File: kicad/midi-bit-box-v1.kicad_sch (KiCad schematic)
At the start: 60 parts, among them IC1 LM386, IC2 DIP14, K1 TQ2-L-5V, Q1 2N3904, Q2 2N3906, Q3 2N3904, Q4 2N3904, U1 AY-3-8910, U2 L78L09_TO92, U3 NE555P

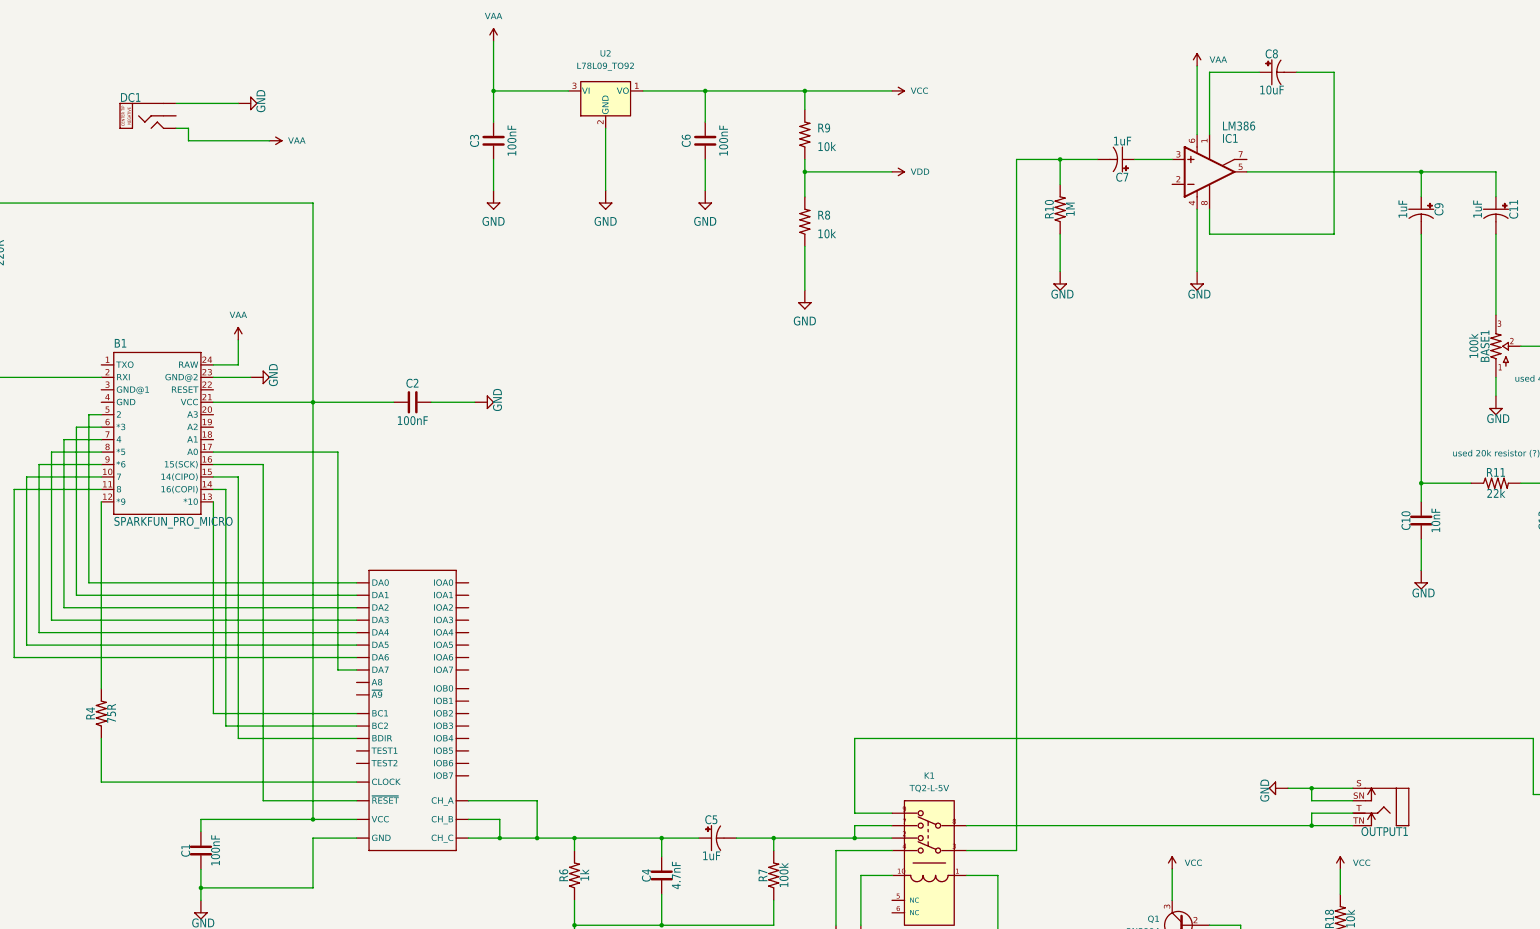
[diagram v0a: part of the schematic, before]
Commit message: Add files via upload
updated pwr/audio jacks and design rules
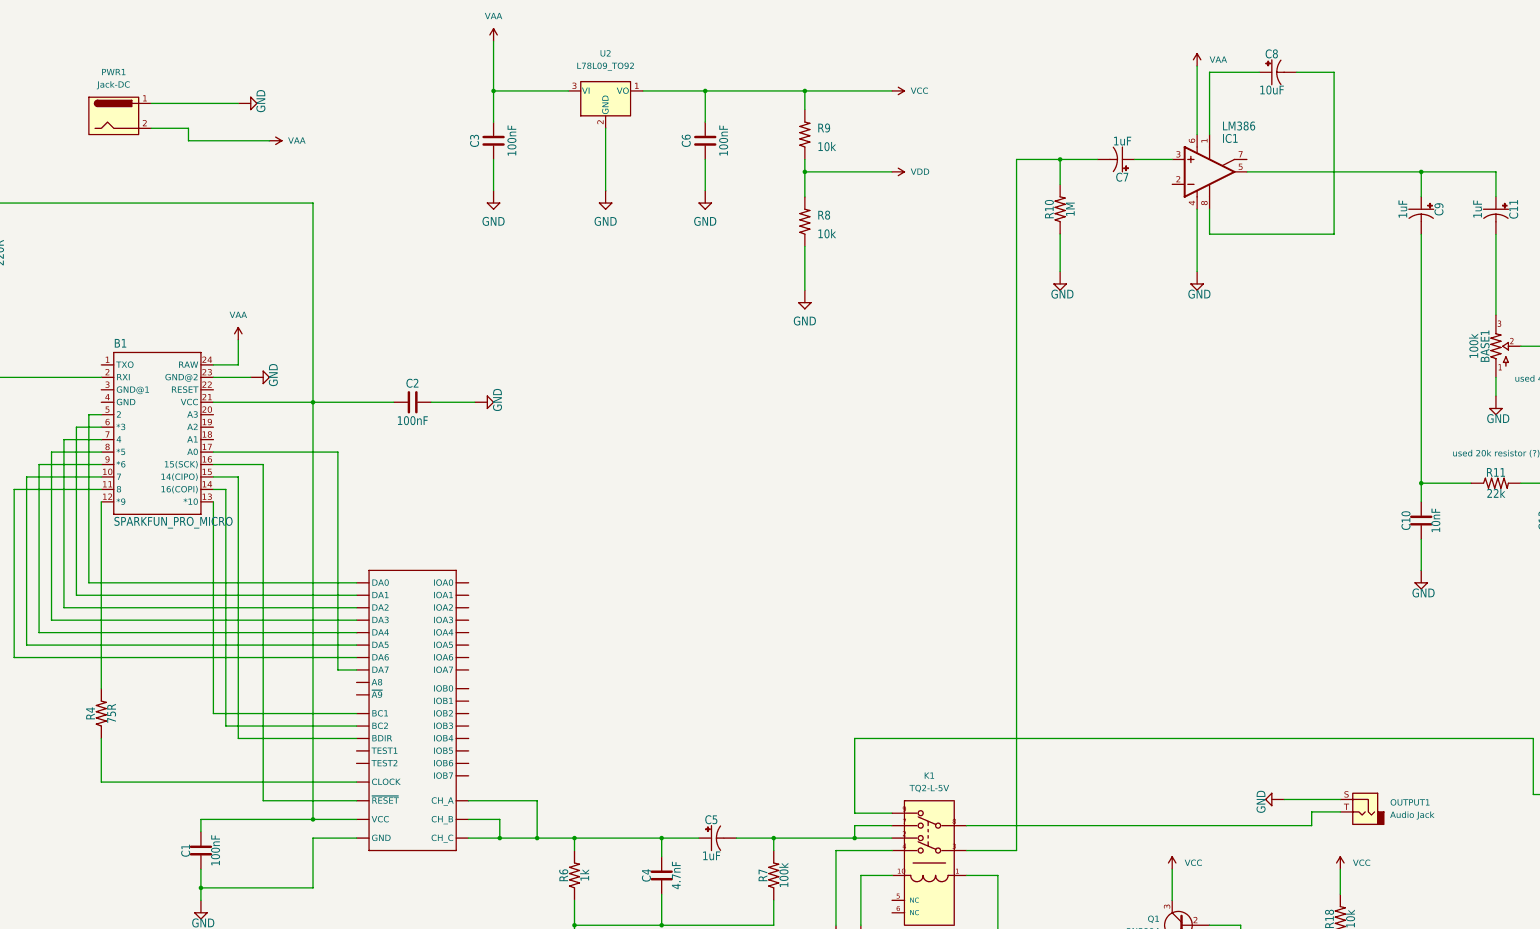
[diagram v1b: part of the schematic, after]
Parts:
- removed DC1: DC_TRS_PADS, midi-bit-box-v1:DC_TRS, symbol midi-bit-box-v1-eagle-import:DC_TRS_PADS
- removed OUTPUT1: SWITCHED_MONO_PADS, midi-bit-box-v1:4PADS, symbol midi-bit-box-v1-eagle-import:SWITCHED_MONO_PADS
- added OUTPUT1: Audio Jack, midi-bit-box-v1:2PADS, symbol Connector:AudioJack2
- added PWR1: Jack-DC, midi-bit-box-v1:DC_TS, symbol Connector:Jack-DC
- Q1, Q2, Q3, Q4, U2: footprint Package_TO_SOT_THT:TO-92_Inline -> midi-bit-box-v1:TO-92-djk-custom
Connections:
- net GND: now also OUTPUT1.S, PWR1.1
- net VAA: now also PWR1.2
- net at K1.8: now also OUTPUT1.T

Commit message: added dual LED
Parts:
- removed D5: LED.2, midi-bit-box-v1:3MM_1, symbol midi-bit-box-v1-eagle-import:LED.2
- added D2: LED_Dual_KAK, LED_THT:LED_D5.0mm-3, symbol Device:LED_Dual_KAK
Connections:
- net GND: now also D2.1 (K1)
- net at R17.1: now also D2.2 (A)
- net at Q4.3 (C): now also D2.3 (K2)
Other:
- moved on the sheet: R17
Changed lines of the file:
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@@
+    (stroke (width 0) (type default) (color 0 0 0 0))
+  )
+  (wire (pts (xy 375.666 244.856) (xy 397.51 244.856))
     (stroke (width 0) (type default) (color 0 0 0 0))
   )
@@
     (stroke (width 0) (type default) (color 0 0 0 0))
   )
-  (wire (pts (xy 342.9 245.11) (xy 355.6 245.11))
+  (wire (pts (xy 331.978 242.316) (xy 344.678 242.316))
     (stroke (width 0) (type default) (color 0 0 0 0))
   )
@@
     (stroke (width 0) (type default) (color 0 0 0 0))
   )
-  (wire (pts (xy 365.76 245.11) (xy 375.92 245.11))
-    (stroke (width 0) (type default) (color 0 0 0 0))
-  )
   (wire (pts (xy 139.7 120.65) (xy 139.7 86.36))
     (stroke (width 0) (type default) (color 0 0 0 0))
@@
     (stroke (width 0) (type default) (color 0 0 0 0))
   )
+  (wire (pts (xy 354.838 242.316) (xy 360.426 242.316))
+    (stroke (width 0) (type default) (color 0 0 0 0))
+  )
   (wire (pts (xy 196.85 130.81) (xy 129.54 130.81))
     (stroke (width 0) (type default) (color 0 0 0 0))
@@
     (stroke (width 0) (type default) (color 0 0 0 0))
   )
-  (wire (pts (xy 397.51 245.11) (xy 397.51 248.92))
+  (wire (pts (xy 397.51 244.856) (xy 397.51 248.92))
     (stroke (width 0) (type default) (color 0 0 0 0))
   )
@@
     (stroke (width 0) (type default) (color 0 0 0 0))
   )
+  (wire (pts (xy 375.666 239.776) (xy 382.778 239.776))
+    (stroke (width 0) (type default) (color 0 0 0 0))
+  )
   (wire (pts (xy 490.22 181.61) (xy 506.73 181.61))
     (stroke (width 0) (type default) (color 0 0 0 0))
@@
   )
   (wire (pts (xy 436.88 161.29) (xy 436.88 149.86))
-    (stroke (width 0) (type default) (color 0 0 0 0))
-  )
-  (wire (pts (xy 383.54 245.11) (xy 397.51 245.11))
     (stroke (width 0) (type default) (color 0 0 0 0))
   )
@@
     (pin "2")
   )
-  (symbol (lib_id "midi-bit-box-v1-eagle-import:LED.2") (at 381 245.11 180) (unit 1)
-    (in_bom yes) (on_board yes) (fields_autoplaced)
-    (property "Reference" "D5" (id 0) (at 380.0856 241.3 0)
-      (effects (font (size 1.778 1.5113)))
-    )
-    (property "Value" "LED.2" (id 1) (at 381 245.11 0)
-      (effects (font (size 1.27 1.27)) hide)
-    )
-    (property "Footprint" "midi-bit-box-v1:3MM_1" (id 2) (at 381 245.11 0)
-      (effects (font (size 1.27 1.27)) hide)
-    )
-    (property "Datasheet" "" (id 3) (at 381 245.11 0)
-      (effects (font (size 1.27 1.27)) hide)
-    )
-    (pin "A")
-    (pin "K")
-  )
   (symbol (lib_id "midi-bit-box-v1-eagle-import:R.3B") (at 281.94 177.8 90) (unit 1)
     (in_bom yes) (on_board yes)
@@
     (pin "2")
   )
-  (symbol (lib_id "power:VCC") (at 342.9 245.11 90) (unit 1)
-    (in_bom yes) (on_board yes)
-    (property "Reference" "#PWR06" (id 0) (at 346.71 245.11 0)
-      (effects (font (size 1.27 1.27)) hide)
-    )
-    (property "Value" "VCC" (id 1) (at 339.09 242.57 90)
+  (symbol (lib_id "power:VCC") (at 331.978 242.316 90) (unit 1)
+    (in_bom yes) (on_board yes)
+    (property "Reference" "#PWR06" (id 0) (at 335.788 242.316 0)
+      (effects (font (size 1.27 1.27)) hide)
+    )
+    (property "Value" "VCC" (id 1) (at 328.168 239.776 90)
       (effects (font (size 1.27 1.27)) (justify right))
     )
-    (property "Footprint" "" (id 2) (at 342.9 245.11 0)
-      (effects (font (size 1.27 1.27)) hide)
-    )
-    (property "Datasheet" "" (id 3) (at 342.9 245.11 0)
+    (property "Footprint" "" (id 2) (at 331.978 242.316 0)
+      (effects (font (size 1.27 1.27)) hide)
+    )
+    (property "Datasheet" "" (id 3) (at 331.978 242.316 0)
       (effects (font (size 1.27 1.27)) hide)
     )
@@
     (pin "7")
   )
-  (symbol (lib_id "midi-bit-box-v1-eagle-import:R.3B") (at 360.68 245.11 180) (unit 1)
-    (in_bom yes) (on_board yes)
-    (property "Reference" "R17" (id 0) (at 360.68 247.2436 0)
-      (effects (font (size 1.778 1.5113)))
-    )
-    (property "Value" "4.7k" (id 1) (at 360.68 242.951 0)
-      (effects (font (size 1.778 1.5113)))
-    )
-    (property "Footprint" "midi-bit-box-v1:0.3_.B" (id 2) (at 360.68 245.11 0)
-      (effects (font (size 1.27 1.27)) hide)
-    )
-    (property "Datasheet" "" (id 3) (at 360.68 245.11 0)
+  (symbol (lib_id "midi-bit-box-v1-eagle-import:R.3B") (at 349.758 242.316 180) (unit 1)
+    (in_bom yes) (on_board yes)
+    (property "Reference" "R17" (id 0) (at 349.758 244.4496 0)
+      (effects (font (size 1.778 1.5113)))
+    )
+    (property "Value" "4.7k" (id 1) (at 349.758 240.157 0)
+      (effects (font (size 1.778 1.5113)))
+    )
+    (property "Footprint" "midi-bit-box-v1:0.3_.B" (id 2) (at 349.758 242.316 0)
+      (effects (font (size 1.27 1.27)) hide)
+    )
+    (property "Datasheet" "" (id 3) (at 349.758 242.316 0)
       (effects (font (size 1.27 1.27)) hide)
     )
@@
     )
     (property "Datasheet" "" (id 3) (at 172.72 68.58 0)
+      (effects (font (size 1.27 1.27)) hide)
+    )
+    (pin "1")
+  )
+  (symbol (lib_id "midi-bit-box-v1-eagle-import:GND") (at 385.318 239.776 90) (unit 1)
+    (in_bom yes) (on_board yes)
+    (property "Reference" "#GND07" (id 0) (at 385.318 239.776 0)
+      (effects (font (size 1.27 1.27)) hide)
+    )
+    (property "Value" "GND" (id 1) (at 388.493 241.681 0)
+      (effects (font (size 1.778 1.5113)) (justify left bottom))
+    )
+    (property "Footprint" "midi-bit-box-v1:" (id 2) (at 385.318 239.776 0)
+      (effects (font (size 1.27 1.27)) hide)
+    )
+    (property "Datasheet" "" (id 3) (at 385.318 239.776 0)
       (effects (font (size 1.27 1.27)) hide)
     )
@@
     (pin "3")
   )
+  (symbol (lib_id "Device:LED_Dual_KAK") (at 368.046 242.316 0) (unit 1)
+    (in_bom yes) (on_board yes) (fields_autoplaced)
+    (property "Reference" "D2" (id 0) (at 368.1095 230.124 0))
+    (property "Value" "LED_Dual_KAK" (id 1) (at 368.1095 232.664 0))
+    (property "Footprint" "LED_THT:LED_D5.0mm-3" (id 2) (at 369.316 242.316 0)
+      (effects (font (size 1.27 1.27)) hide)
+    )
+    (property "Datasheet" "~" (id 3) (at 369.316 242.316 0)
+      (effects (font (size 1.27 1.27)) hide)
+    )
+    (pin "1")
+    (pin "2")
+    (pin "3")
+  )
   (symbol (lib_id "midi-bit-box-v1-eagle-import:MOUNT-HOLE4.1") (at 20.32 76.2 0) (unit 1)
     (in_bom yes) (on_board yes)
@@
       (reference "#GND06") (unit 1) (value "GND") (footprint "midi-bit-box-v1:")
     )
+    (path "/bcca330a-fb71-48b9-b450-fdd71bedbb8f"
+      (reference "#GND07") (unit 1) (value "GND") (footprint "midi-bit-box-v1:")
+    )
     (path "/f80a85fd-e6d4-41d6-ba9f-12f575651e85"
       (reference "#GND08") (unit 1) (value "GND") (footprint "midi-bit-box-v1:")
@@
       (reference "D1") (unit 1) (value "1N4148") (footprint "midi-bit-box-v1:DO41-3")
     )
-    (path "/4928e3da-bd7b-4282-b856-3afc1c50ffef"
-      (reference "D5") (unit 1) (value "LED.2") (footprint "midi-bit-box-v1:3MM_1")
+    (path "/ef4cf6d5-46f8-4205-84c4-c020af9e3cbb"
+      (reference "D2") (unit 1) (value "LED_Dual_KAK") (footprint "LED_THT:LED_D5.0mm-3")
     )
     (path "/7fd7cb09-496d-4f85-a95b-f531a0ea6ec8"
